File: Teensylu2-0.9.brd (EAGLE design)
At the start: 101.6 x 76.2 mm, 113 parts, among them J1 12VPWR, J10 HOTEND-2, J11 E1-THRM, J12 B-THRM, J13 E2-THRM, J2 MICROSD, J3 USB-MICRO-PTH, J4 FAN, J5 4P-TERM-BLOCK284391-4, J6 39-29-3066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

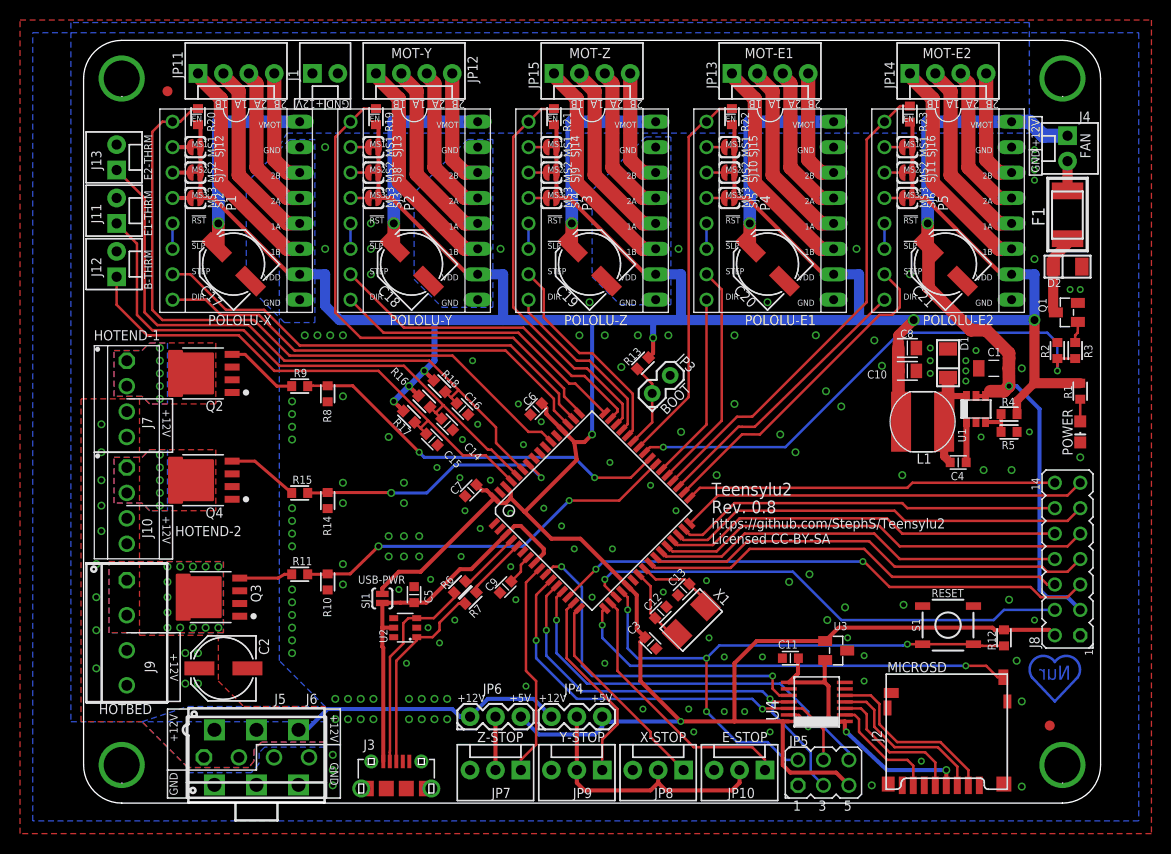
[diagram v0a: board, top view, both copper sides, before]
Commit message: Production release
Pin mapping is added. Had to move a lot of pins around due to limitation
of the Teensyduino library.
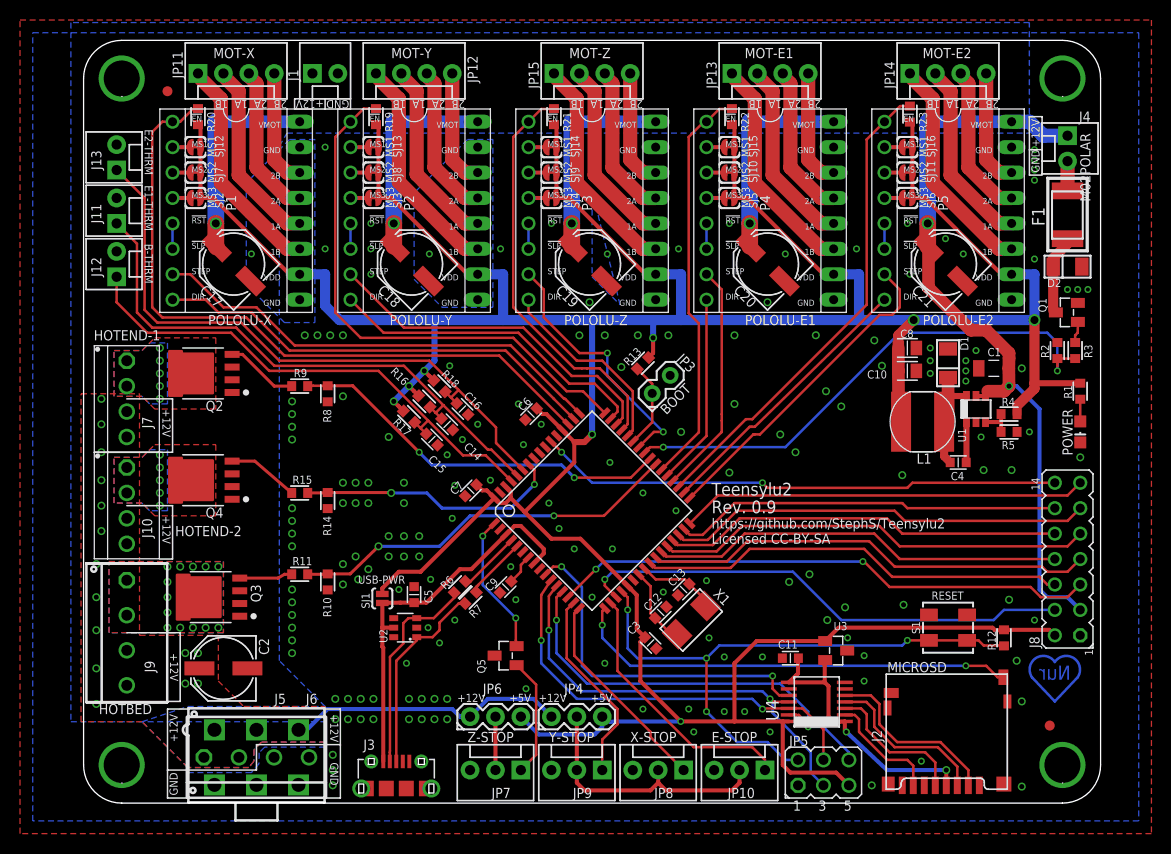
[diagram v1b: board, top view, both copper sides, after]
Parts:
- added Q5: MMUN2211LT3G, teensylu:SOT23C
- C5: value 0.1uf -> 0.1uF
- C9: value 1uf -> 1uF
- J1: value 12VPWR -> M02POLAR
- J11: value E1-THRM -> M02POLAR
- J12: value B-THRM -> M02POLAR
- J13: value E2-THRM -> M02POLAR
- J4: value FAN -> M02POLAR
- JP10: value E-STOP -> M03POLAR
- JP4: value X-STOP-VOLTAGE -> JUMPER-3PTH
- JP6: value Z-STOP-VOLTAGE -> JUMPER-3PTH
- JP7: value Z-STOP -> M03POLAR
- JP8: value X-STOP -> M03POLAR
- JP9: value Y-STOP -> M03POLAR
- R5: value 6.49 -> 6.49k
- moved C6 0.72 mm to (44.7, 38.9)
- moved S1 0.25 mm to (86.4, 17.5)
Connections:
- removed net PE0: J8.14, U5.33
- removed net PE6: U5.1
- new net A7: J8.14, U5.54
- new net PE3: U5.9
- new net Z-STOP-BIAS: JP7.1, Q5.1
- net !E1-ENABLE: now also U5.38; no longer U5.42
- net !E2-ENABLE: now also U5.35; no longer U5.36
- net !X-ENABLE: now also U5.51; no longer U5.54
- net !Y-ENABLE: now also U5.48; no longer U5.49
- net !Z-ENABLE: now also U5.45; no longer U5.46
- net E1-DIR: now also U5.37; no longer U5.38
- net E1-STEP: now also U5.36; no longer U5.37
- net E2-DIR: now also U5.34; no longer U5.35
- net E2-STEP: now also U5.33; no longer U5.34
- net GND: now also Q5.3
- net X-DIR: now also U5.50; no longer U5.51
- net X-STEP: now also U5.49; no longer U5.50
- net Y-DIR: now also U5.47; no longer U5.48
- net Y-STEP: now also U5.46; no longer U5.47
- net Z-DIR: now also U5.44; no longer U5.45
- net Z-STEP: now also U5.42; no longer U5.44
- net Z-STOP: now also Q5.2, U5.1; no longer JP7.1, U5.9
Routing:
- net A7: track 0.00 -> 52.5 mm, vias 0 -> 2
- net PE0: track 37.1 -> 0.00 mm
- net Z-STOP-BIAS: track 0.00 -> 11.9 mm
- net Z-STOP: track 21.7 -> 14.2 mm, vias 0 -> 2
- net Z-STEP: track 21.4 -> 26.0 mm, vias 0 -> 2
- net Y-DIR: track 30.1 -> 32.6 mm
- net !E1-ENABLE: track 38.6 -> 40.7 mm
- net !Y-ENABLE: track 51.8 -> 53.9 mm
- net Y-STEP: track 33.5 -> 35.0 mm
- net !Z-ENABLE: track 39.5 -> 41.0 mm
- net Z-DIR: track 18.1 -> 19.6 mm
- net !X-ENABLE: track 68.6 -> 69.4 mm
- net SCLK: track 43.2 -> 42.6 mm
- net 12V: track 187.3 -> 187.6 mm, vias 19 -> 21
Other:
- board text added: "B-THRM"
- board text added: "E-STOP"
- board text added: "E1-THRM"
- board text added: "E2-THRM"
- board text added: "Rev. 0.9"
- board text added: "X-STOP"
- board text added: "Y-STOP"
- board text added: "Z-STOP"
- board text removed: "Rev. 0.8"
